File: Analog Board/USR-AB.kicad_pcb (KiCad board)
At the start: 2 copper layers, 129.5 x 61.1 mm, 120 parts, among them J2 S5B-XH-A_LF__SN_, J3 S5B-XH-A_LF__SN_, U2 CD74HC4067SM96, U3 SC0918

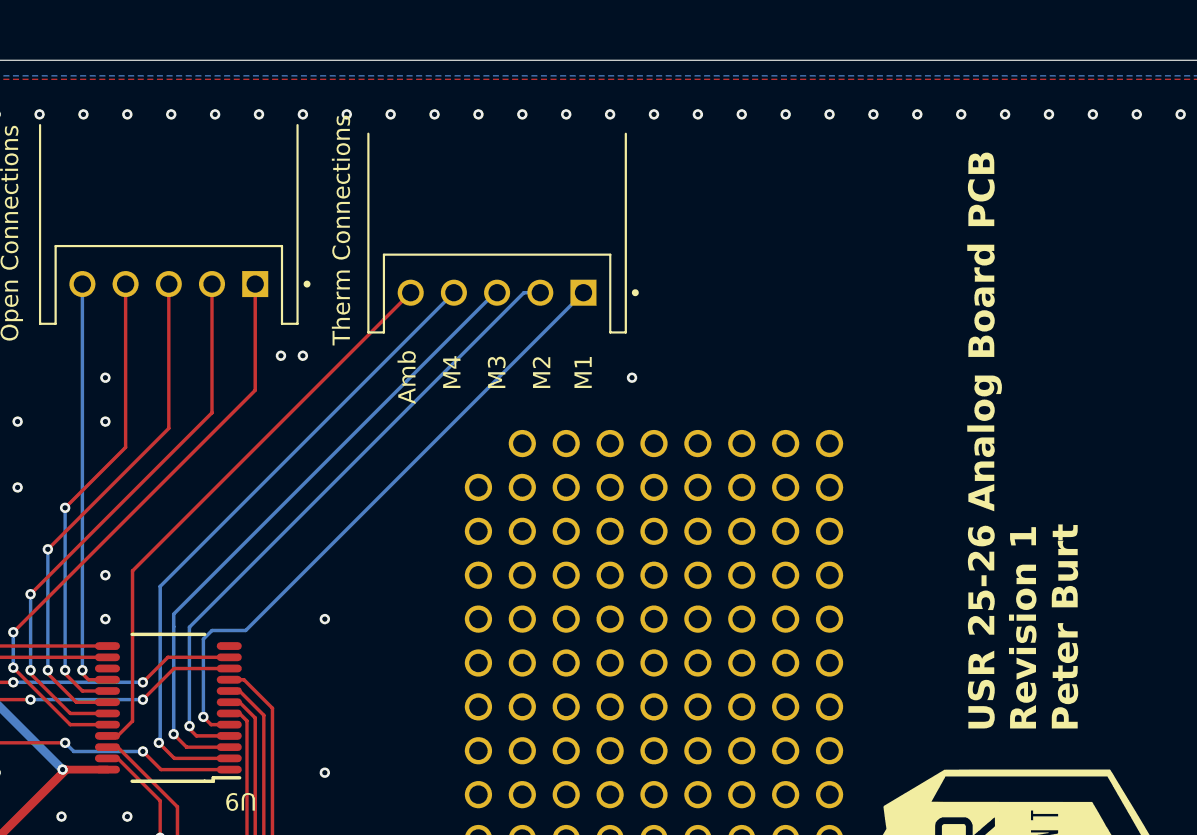
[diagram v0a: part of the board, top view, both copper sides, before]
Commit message: Updated PCB designs across the motor driver, analog board, and PDB
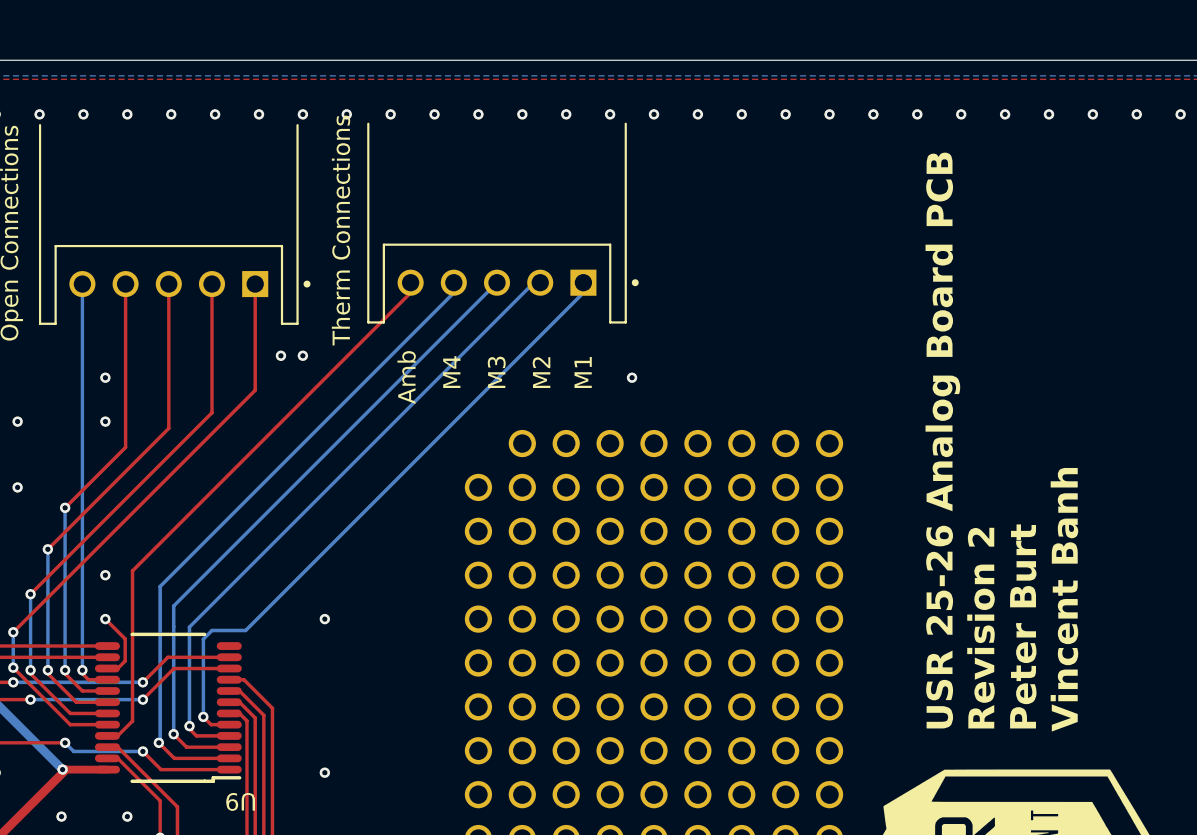
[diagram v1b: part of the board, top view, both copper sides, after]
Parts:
- moved J2 0.58 mm to (123.0, 91.7)
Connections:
- U2 pad 15: unconnected-(U2-E_N-Pad15) -> GND
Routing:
- net GND: track 13.0 -> 17.1 mm
- net M2_THERM: track 36.8 -> 37.6 mm
- net M4_THERM: track 37.6 -> 38.1 mm
- net AMB_THERM: track 33.3 -> 33.8 mm
- net M1_THERM: track 36.5 -> 37.1 mm
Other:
- board text added: "May need to connect pin 15 of MUX (Enable) up to a Pico pin"
- board text added: "USR 25-26 Analog Board PCB Revision 2 Peter Burt Vincent Banh"
- board text removed: "USR 25-26 Analog Board PCB Revision 1 Peter Burt"
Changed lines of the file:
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@@
 		(title "Analog Board 2025-2026")
 		(date "2026-03-24")
+		(rev "2")
 		(company "Utah Student Robotics")
 		(comment 1 "Peter Burt")
@@
 			(size 0.449999 1.45)
 			(layers "F.Cu" "F.Mask" "F.Paste")
-			(net "unconnected-(U2-E_N-Pad15)")
+			(net "GND")
 			(pinfunction "E_N_15")
-			(pintype "input+no_connect")
+			(pintype "input")
 		)
 		(pad "16" smd oval
@@
 	(footprint "USR:JST-XH 5-PIN"
 		(layer "F.Cu")
-		(at 123 92.25 180)
+		(at 122.995838 91.670987 180)
 		(property "Reference" "J2"
 			(at -4.445 -10.795 0)
@@
 		)
 	)
-	(gr_text "USR 25-26 Analog Board PCB\nRevision 1\nPeter Burt"
+	(gr_text "USR 25-26 Analog Board PCB\nRevision 2\nPeter Burt\nVincent Banh"
 		(at 156.7867 123.3596 90)
 		(layer "F.SilkS")
@@
 		)
 	)
+	(gr_text "May need to connect pin 15 of MUX (Enable) up to a Pico pin"
+		(at 88.9 157.48 0)
+		(layer "User.1")
+		(effects
+			(font
+				(size 1.5 1.5)
+				(thickness 0.3)
+				(bold yes)
+			)
+			(justify left bottom)
+		)
+	)
 	(dimension
 		(type orthogonal)
@@
 	)
 	(segment
-		(start 103.5 114.95)
-		(end 120.5 97.95)
+		(start 103.5 123.92533)
+		(end 103.5 114.95)
 		(width 0.2)
 		(layer "B.Cu")
@@
 	)
 	(segment
-		(start 103.5 123.92533)
-		(end 103.5 114.95)
+		(start 120.495838 97.954162)
+		(end 120.495838 97.370987)
 		(width 0.2)
 		(layer "B.Cu")
@@
 	)
 	(segment
+		(start 103.5 114.95)
+		(end 120.495838 97.954162)
+		(width 0.2)
+		(layer "B.Cu")
+		(net "M4_THERM")
+	)
+	(segment
 		(start 105.030977 124.251351)
 		(end 104.280976 123.50135)
@@
 	)
 	(segment
-		(start 104.282989 117.278963)
+		(start 104.282989 116.083836)
+		(end 122.81257 97.554255)
+		(width 0.2)
+		(layer "B.Cu")
+		(net "M3_THERM")
+	)
+	(segment
+		(start 104.280976 123.50135)
 		(end 104.280976 117.280976)
 		(width 0.2)
@@
 	)
 	(segment
-		(start 104.282989 116.554255)
-		(end 104.282989 117.278963)
+		(start 122.81257 97.554255)
+		(end 123.282989 97.554255)
 		(width 0.2)
 		(layer "B.Cu")
@@
 	)
 	(segment
-		(start 104.280976 123.50135)
-		(end 104.280976 117.280976)
+		(start 104.282989 117.278963)
+		(end 104.282989 116.083836)
 		(width 0.2)
 		(layer "B.Cu")
@@
 	)
 	(segment
-		(start 104.282989 116.554255)
-		(end 123.282989 97.554255)
+		(start 104.280976 117.280976)
+		(end 104.282989 117.278963)
 		(width 0.2)
 		(layer "B.Cu")
@@
 	)
 	(segment
-		(start 124.55 97.95)
+		(start 105.193763 117.306237)
+		(end 105.193763 123.051333)
+		(width 0.2)
+		(layer "B.Cu")
+		(net "M2_THERM")
+	)
+	(segment
+		(start 125.129013 97.370987)
 		(end 105.193763 117.306237)
 		(width 0.2)
@@
 	(segment
 		(start 125.5 97.95)
-		(end 124.55 97.95)
+		(end 125.5 97.375149)
 		(width 0.2)
 		(layer "B.Cu")
@@
 	)
 	(segment
-		(start 105.193763 117.306237)
-		(end 105.193763 123.051333)
+		(start 125.495838 97.370987)
+		(end 125.129013 97.370987)
+		(width 0.2)
+		(layer "B.Cu")
+		(net "M2_THERM")
+	)
+	(segment
+		(start 125.5 97.375149)
+		(end 125.495838 97.370987)
 		(width 0.2)
 		(layer "B.Cu")
@@
 	)
 	(segment
-		(start 106 118)
-		(end 106.5 117.5)
+		(start 106.5 117.5)
+		(end 108.45 117.5)
 		(width 0.2)
 		(layer "B.Cu")
@@
 	)
 	(segment
-		(start 106.5 117.5)
-		(end 108.45 117.5)
+		(start 106 118)
+		(end 106.5 117.5)
 		(width 0.2)
 		(layer "B.Cu")
@@
 	(segment
 		(start 108.45 117.5)
-		(end 128 97.95)
+		(end 127.995838 97.954162)
+		(width 0.2)
+		(layer "B.Cu")
+		(net "M1_THERM")
+	)
+	(segment
+		(start 127.995838 97.954162)
+		(end 127.995838 97.370987)
 		(width 0.2)
 		(layer "B.Cu")
@@
 	)
 	(segment
+		(start 101.474999 119.267464)
+		(end 101.474999 117.984999)
+		(width 0.2)
+		(layer "F.Cu")
+		(net "GND")
+	)
+	(segment
+		(start 100.449999 119.7)
+		(end 101.042463 119.7)
+		(width 0.2)
+		(layer "F.Cu")
+		(net "GND")
+	)
+	(segment
 		(start 124.62 147.02)
 		(end 122.2 144.6)
@@
 	)
 	(segment
+		(start 101.042463 119.7)
+		(end 101.474999 119.267464)
+		(width 0.2)
+		(layer "F.Cu")
+		(net "GND")
+	)
+	(segment
 		(start 117 150)
 		(end 117 143.4)
@@
 		(net "GND")
 	)
+	(segment
+		(start 101.474999 117.984999)
+		(end 100.33 116.84)
+		(width 0.2)
+		(layer "F.Cu")
+		(net "GND")
+	)
 	(via
 		(at 165.1 97.79)
@@
 	)
 	(segment
-		(start 101.9 122.742462)
-		(end 101.9 114.05)
+		(start 101.042462 123.6)
+		(end 101.9 122.742462)
 		(width 0.2)
 		(layer "F.Cu")
@@
 	)
 	(segment
-		(start 101.042462 123.6)
-		(end 101.9 122.742462)
+		(start 100.449999 123.6)
+		(end 101.042462 123.6)
 		(width 0.2)
 		(layer "F.Cu")
@@
 	)
 	(segment
-		(start 100.449999 123.6)
-		(end 101.042462 123.6)
+		(start 117.995838 97.954162)
+		(end 117.995838 97.370987)
 		(width 0.2)
 		(layer "F.Cu")
@@
 	(segment
 		(start 101.9 114.05)
-		(end 118 97.95)
+		(end 117.995838 97.954162)
+		(width 0.2)
+		(layer "F.Cu")
+		(net "AMB_THERM")
+	)
+	(segment
+		(start 101.9 122.742462)
+		(end 101.9 114.05)
 		(width 0.2)
 		(layer "F.Cu")
